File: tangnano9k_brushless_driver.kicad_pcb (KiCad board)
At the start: 2 copper layers, 81.5 x 99.9 mm, 27 parts, among them CN1 Nucleo_F302R8, J2 01x08_Socket, J3 01x04_Socket, SW2 SW_SPDT, SW3 SW_SPDT, U1 Tang_Nano_9k_board, U2 MCP3008, U3 C-574SR-LF

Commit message: 0925
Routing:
- net +3V3: track 126.8 -> 125.1 mm
- net GND: vias 13 -> 16
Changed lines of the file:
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@@
   (via (at 167.64 138.684) (size 0.8) (drill 0.4) (layers "F.Cu" "B.Cu") (free) (net 1))
   (via (at 147.066 146.05) (size 0.8) (drill 0.4) (layers "F.Cu" "B.Cu") (free) (net 1))
+  (via (at 146.558 103.886) (size 0.8) (drill 0.4) (layers "F.Cu" "B.Cu") (free) (net 1))
   (via (at 190.5 81.28) (size 0.8) (drill 0.4) (layers "F.Cu" "B.Cu") (free) (net 1))
   (via (at 195.326 149.098) (size 0.8) (drill 0.4) (layers "F.Cu" "B.Cu") (free) (net 1))
@@
   (via (at 147.066 132.334) (size 0.8) (drill 0.4) (layers "F.Cu" "B.Cu") (free) (net 1))
   (via (at 195.326 141.224) (size 0.8) (drill 0.4) (layers "F.Cu" "B.Cu") (free) (net 1))
+  (via (at 149.225 103.886) (size 0.8) (drill 0.4) (layers "F.Cu" "B.Cu") (free) (net 1))
+  (via (at 143.764 103.886) (size 0.8) (drill 0.4) (layers "F.Cu" "B.Cu") (free) (net 1))
   (via (at 186.436 131.826) (size 0.8) (drill 0.4) (layers "F.Cu" "B.Cu") (free) (net 1))
   (via (at 196.85 76.708) (size 0.8) (drill 0.4) (layers "F.Cu" "B.Cu") (free) (net 1))
@@
   (segment (start 159.766 147.828) (end 160.0631 147.828) (width 0.25) (layer "B.Cu") (net 16))
   (segment (start 125.984 108.458) (end 125.984 146.304) (width 0.25) (layer "B.Cu") (net 16))
-  (segment (start 143.764 104.648) (end 160.0631 104.648) (width 1) (layer "F.Cu") (net 17))
-  (segment (start 139.7 107.188) (end 141.224 107.188) (width 1) (layer "F.Cu") (net 17))
+  (segment (start 149.225 107.188) (end 151.765 104.648) (width 1) (layer "F.Cu") (net 17))
+  (segment (start 139.7 107.188) (end 149.225 107.188) (width 1) (layer "F.Cu") (net 17))
   (segment (start 132.08 107.188) (end 139.7 107.188) (width 1) (layer "F.Cu") (net 17))
-  (segment (start 141.224 107.188) (end 143.764 104.648) (width 1) (layer "F.Cu") (net 17))
+  (segment (start 151.765 104.648) (end 160.0631 104.648) (width 1) (layer "F.Cu") (net 17))
   (segment (start 138.684 114.808) (end 139.7 113.792) (width 1) (layer "F.Cu") (net 20))
   (segment (start 139.7 113.792) (end 139.7 112.268) (width 1) (layer "F.Cu") (net 20))
@@
   (segment (start 124.079 60.833) (end 134.097 60.833) (width 0.5) (layer "B.Cu") (net 106))
   (segment (start 120.65 69.342) (end 120.65 61.976) (width 0.5) (layer "B.Cu") (net 106))
+  (segment (start 152.4 101.092) (end 138.684 101.092) (width 0.5) (layer "B.Cu") (net 106))
+  (segment (start 160.0631 89.408) (end 158.620903 89.408) (width 0.5) (layer "B.Cu") (net 106))
   (segment (start 135.255 60.833) (end 135.382 60.706) (width 0.5) (layer "B.Cu") (net 106))
-  (segment (start 154.432 101.092) (end 150.876 104.648) (width 0.5) (layer "B.Cu") (net 106))
   (segment (start 134.097 60.833) (end 134.112 60.848) (width 0.5) (layer "B.Cu") (net 106))
-  (segment (start 150.876 104.648) (end 143.51 104.648) (width 0.5) (layer "B.Cu") (net 106))
   (segment (start 146.431 72.771) (end 124.079 72.771) (width 0.5) (layer "B.Cu") (net 106))
   (segment (start 135.382 60.706) (end 146.558 60.706) (width 0.5) (layer "B.Cu") (net 106))
-  (segment (start 157.734 89.408) (end 154.432 92.71) (width 0.5) (layer "B.Cu") (net 106))
-  (segment (start 143.51 104.648) (end 132.08 104.648) (width 0.5) (layer "B.Cu") (net 106))
-  (segment (start 160.0631 89.408) (end 157.734 89.408) (width 0.5) (layer "B.Cu") (net 106))
+  (segment (start 158.620903 89.544113) (end 154.432 93.733016) (width 0.5) (layer "B.Cu") (net 106))
   (segment (start 149.86 76.2) (end 146.431 72.771) (width 0.5) (layer "B.Cu") (net 106))
+  (segment (start 154.432 93.733016) (end 154.432 99.06) (width 0.5) (layer "B.Cu") (net 106))
+  (segment (start 138.684 101.092) (end 135.128 104.648) (width 0.5) (layer "B.Cu") (net 106))
   (segment (start 134.097 60.833) (end 135.255 60.833) (width 0.5) (layer "B.Cu") (net 106))
+  (segment (start 154.432 99.06) (end 152.4 101.092) (width 0.5) (layer "B.Cu") (net 106))
   (segment (start 149.86 80.01) (end 149.86 76.2) (width 0.5) (layer "B.Cu") (net 106))
   (segment (start 124.079 72.771) (end 120.65 69.342) (width 0.5) (layer "B.Cu") (net 106))
+  (segment (start 135.128 104.648) (end 132.08 104.648) (width 0.5) (layer "B.Cu") (net 106))
+  (segment (start 158.620903 89.408) (end 158.620903 89.544113) (width 0.5) (layer "B.Cu") (net 106))
   (segment (start 121.793 60.833) (end 124.079 60.833) (width 0.5) (layer "B.Cu") (net 106))
-  (segment (start 154.432 92.71) (end 154.432 101.092) (width 0.5) (layer "B.Cu") (net 106))
   (segment (start 120.65 61.976) (end 121.793 60.833) (width 0.5) (layer "B.Cu") (net 106))
   (segment (start 146.939 63.373) (end 166.751 83.185) (width 0.25) (layer "B.Cu") (net 107))

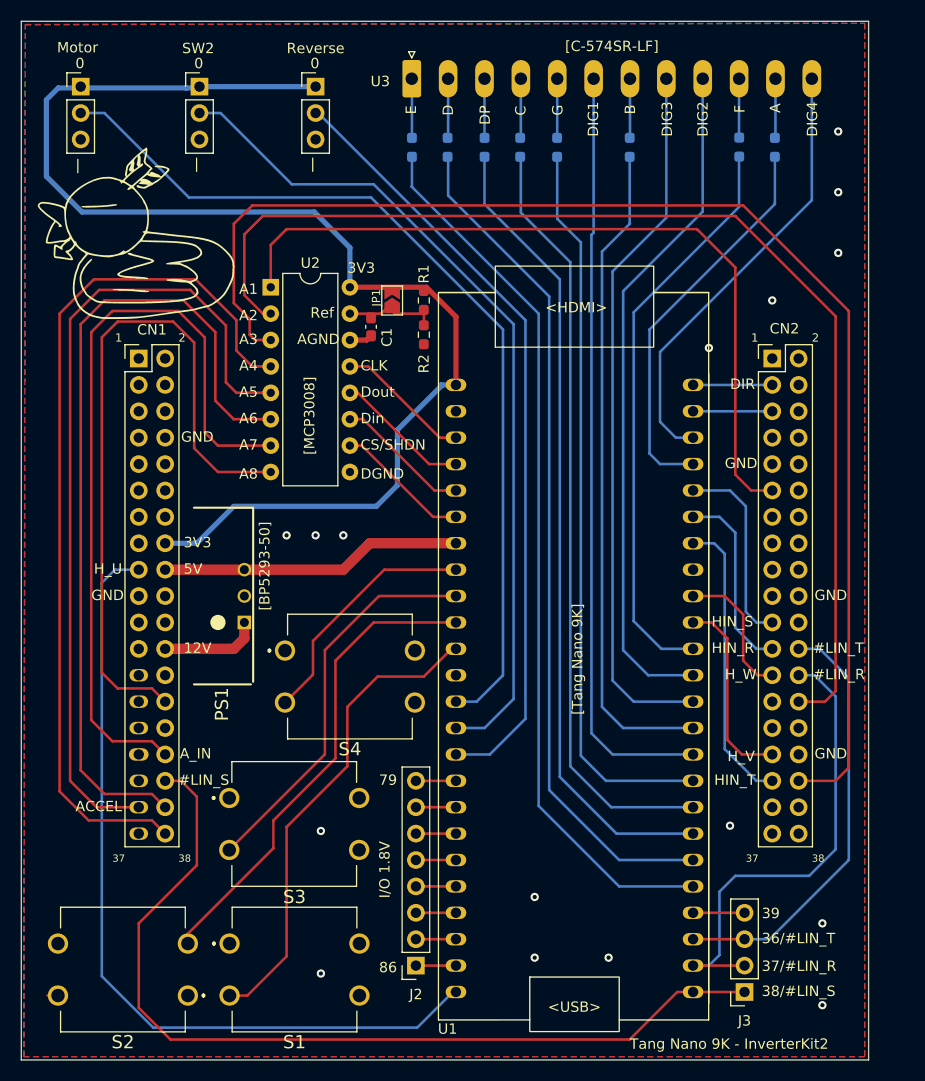
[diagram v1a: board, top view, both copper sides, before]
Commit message: 8seg led footprint fix
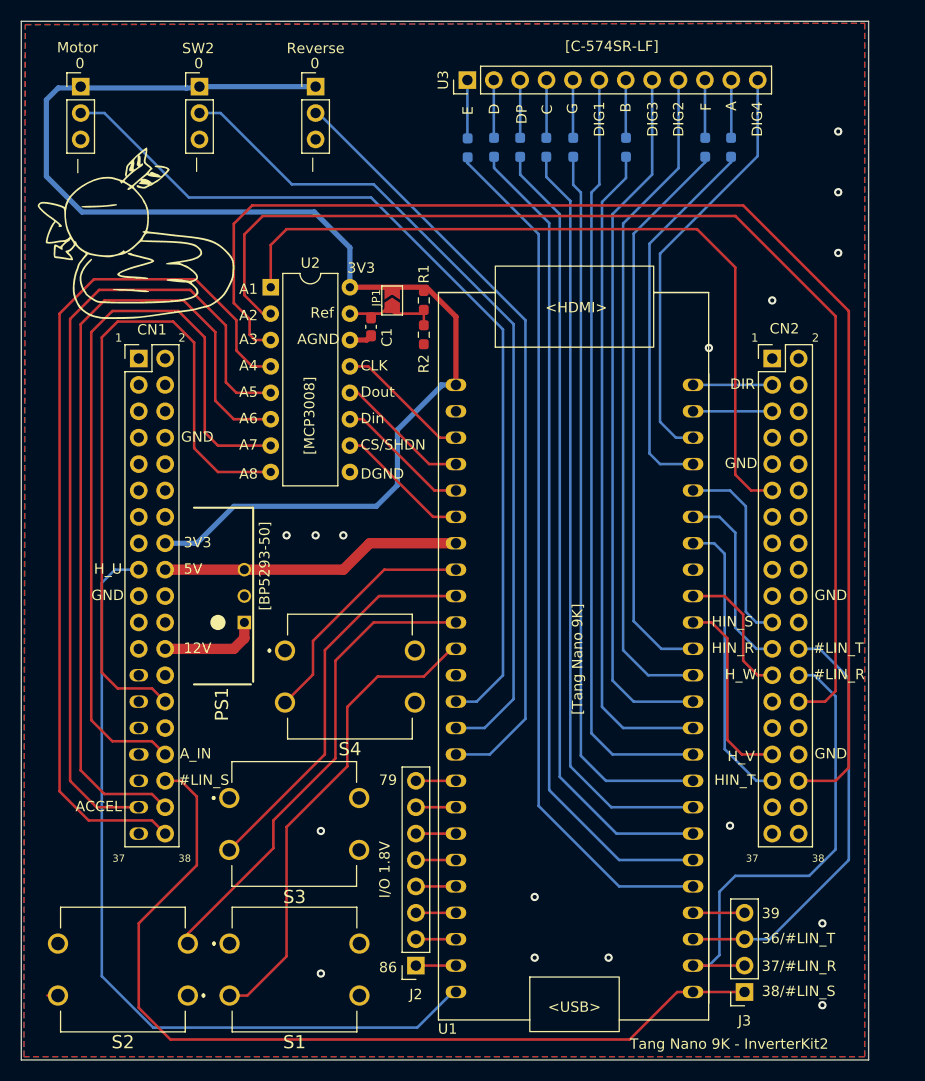
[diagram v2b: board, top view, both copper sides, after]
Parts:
- U3: value C-574SR-LF -> PinHeader_1x12_P2.54mm_Vertical; footprint Library:C-574SR-LF -> Connector_PinHeader_2.54mm:PinHeader_1x12_P2.54mm_Vertical
- moved R3 5.36 mm to (161.2, 66.6)
- moved U3 5.35 mm to (161.2, 60.1), turned to 90 degrees
- moved R4 4.47 mm to (163.7, 66.5)
- moved R9 4.22 mm to (186.5, 66.5)
- moved R5 3.43 mm to (166.2, 66.5)
- moved R10 3.28 mm to (184.0, 66.5)
- moved R6 2.51 mm to (168.8, 66.5)
- moved R7 1.55 mm to (171.3, 66.5)
- moved R8 0.36 mm to (176.4, 66.5)
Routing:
- net Net-(U1-25/IOB8A): track 85.6 -> 83.3 mm
- net /DIG4: track 42.9 -> 40.6 mm
- net Net-(U1-26/IOB8B): track 81.6 -> 79.8 mm
- net /Anode_A: track 38.2 -> 36.4 mm
- net Net-(U1-35/IOB29A/RGB_CK): track 55.7 -> 54.4 mm
- net Net-(U1-27/IOB11A): track 77.8 -> 76.4 mm
- net /DIG2: track 65.9 -> 64.8 mm
- net Net-(U1-28/IOB11B): track 74.1 -> 73.1 mm
- net /DIG3: track 68.6 -> 68.0 mm
- net Net-(U1-29/IOB13A): track 70.4 -> 69.7 mm

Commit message: 1019
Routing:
- net Net-(S2-NO_1): track 46.2 -> 45.1 mm
- net Net-(S3-NO_1): track 37.8 -> 36.8 mm
- net Net-(S4-NO_1): track 23.6 -> 22.8 mm
- net +3V3: track 125.1 -> 125.7 mm
